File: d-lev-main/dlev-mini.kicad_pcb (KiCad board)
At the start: 4 copper layers, 175.3 x 163.3 mm, 126 parts, among them J1 S12B-PH-SM4-TB, J2 Tag-Connect TC2030-NL, J3 S8B-PH-SM4-TB, J4 S8B-PH-SM4-TB, J5 S6B-PH-SM4-TB, Q1 BSS138, Q2 BSS138, Q3 BSS138, Q4 BSS138, Q5 BSS138, SW1 RotaryEncoder_Switch, SW2 RotaryEncoder_Switch, SW3 RotaryEncoder_Switch, SW4 RotaryEncoder_Switch, SW5 RotaryEncoder_Switch, SW6 RotaryEncoder_Switch, SW7 RotaryEncoder_Switch, SW8 RotaryEncoder_Switch, U2 25LCxxx, U3 AC608, U4 AMS1117-3.3

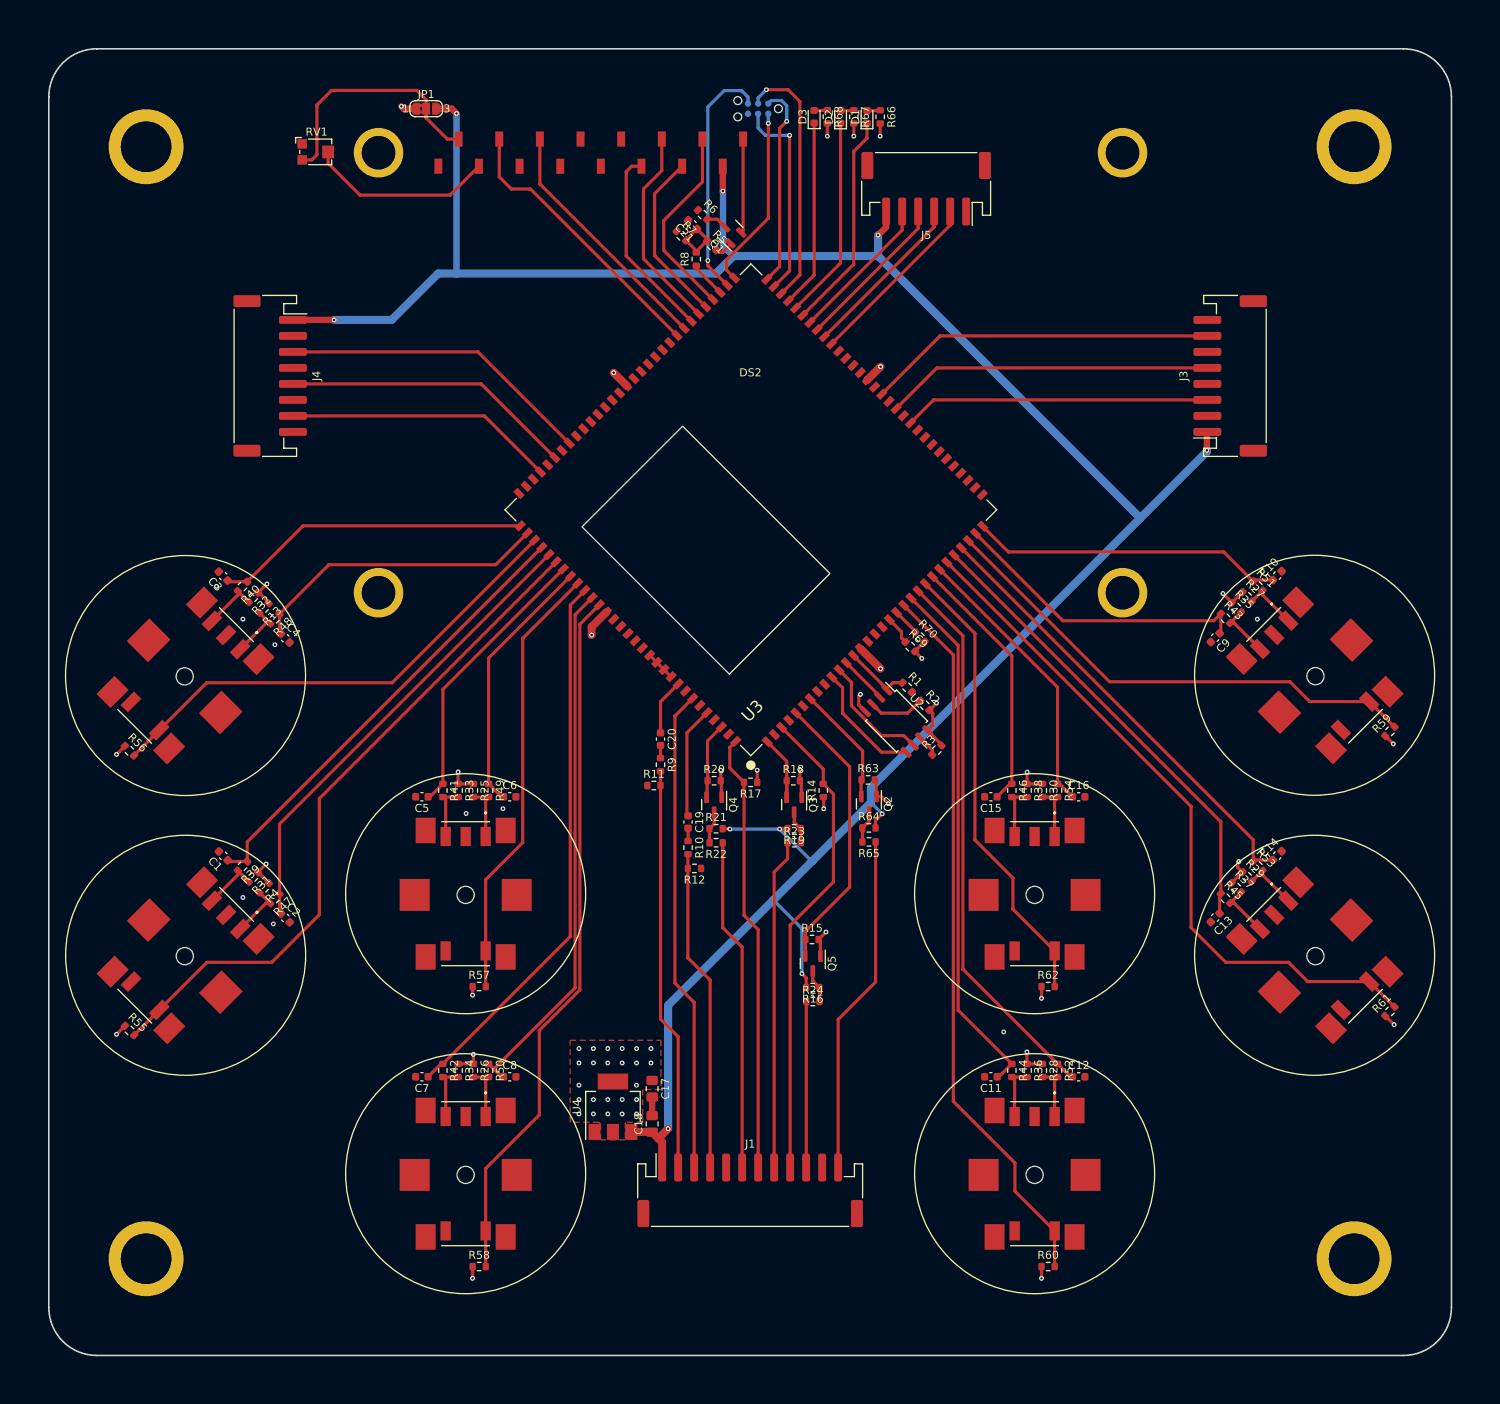
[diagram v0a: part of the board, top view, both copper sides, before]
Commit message: Via stitching around afe traces and add fix for lcd contrast pot
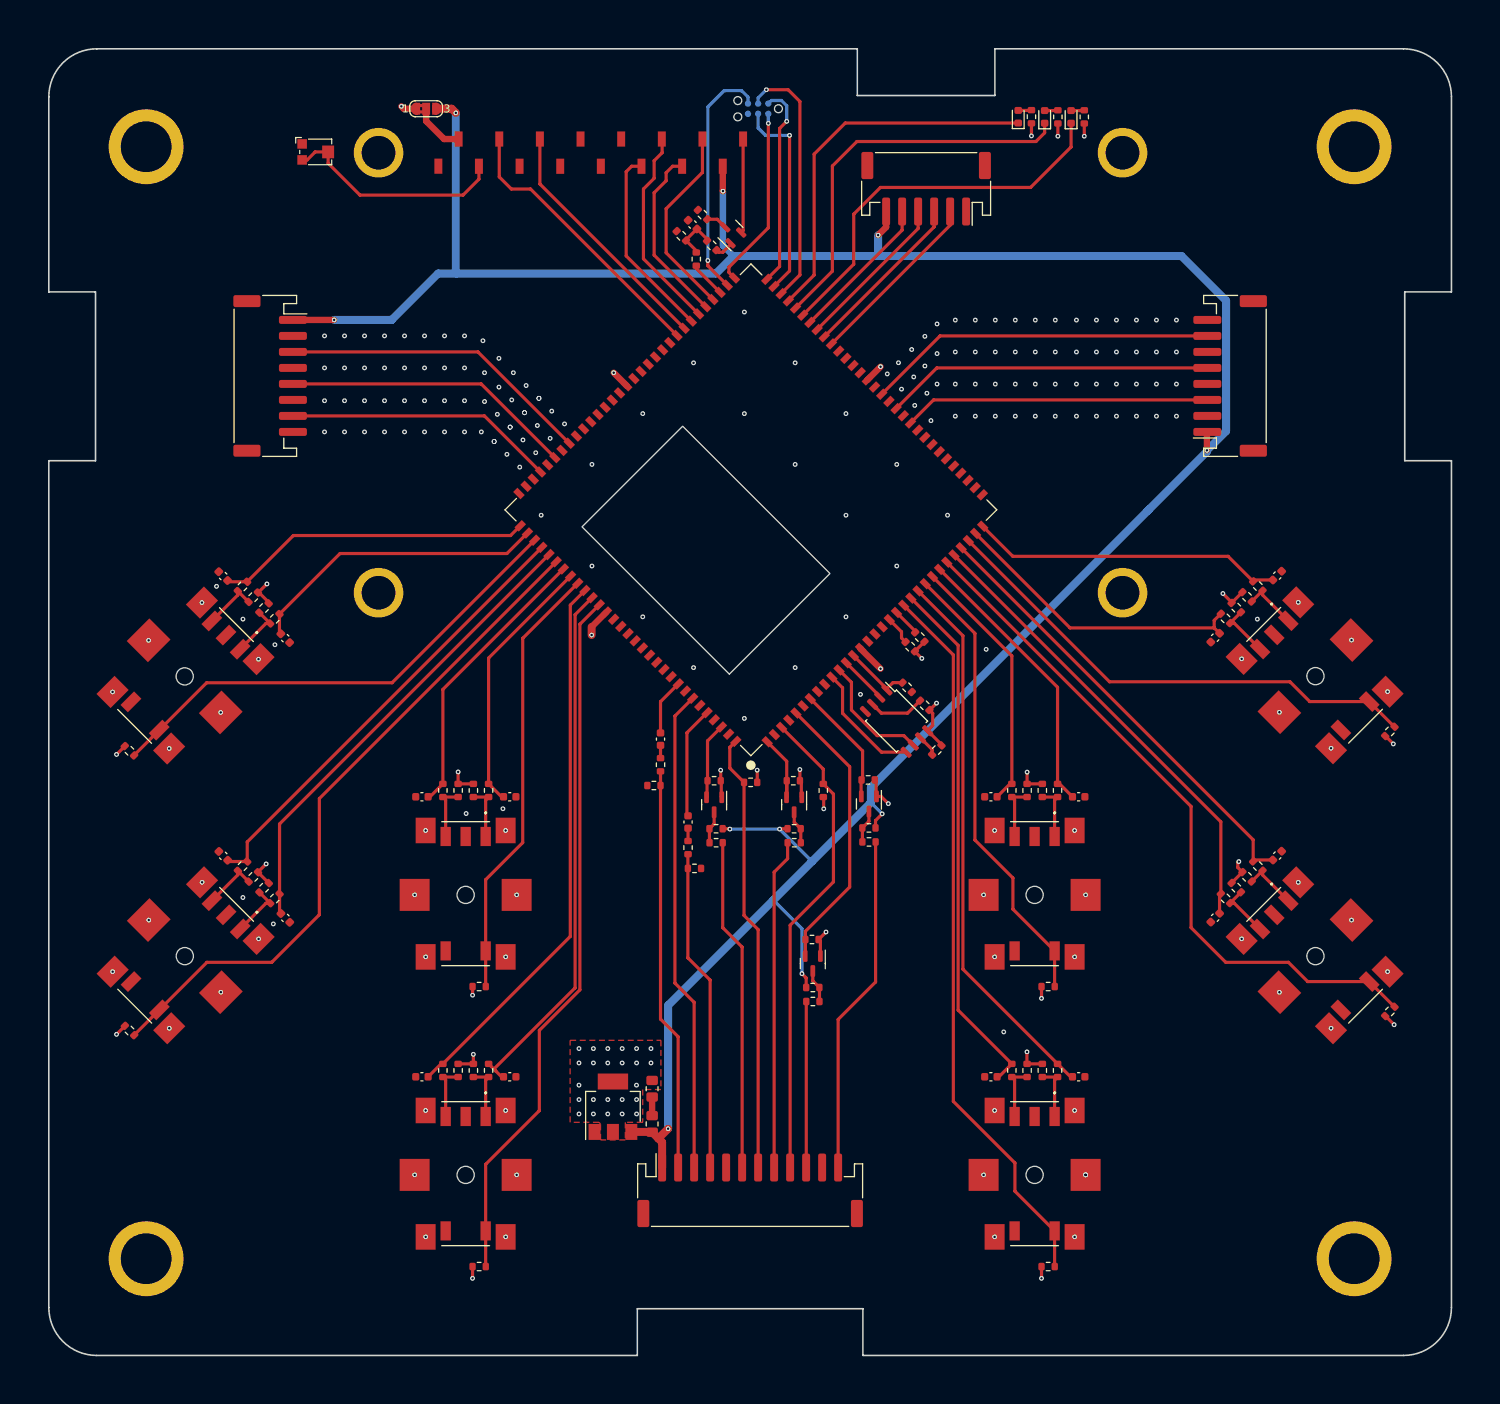
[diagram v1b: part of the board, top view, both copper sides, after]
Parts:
- moved D3 25.5 mm to (33.5, -102.0)
- moved R66 25.5 mm to (41.8, -102.0)
- moved R67 25.5 mm to (38.5, -102.0)
- moved R68 25.5 mm to (35.2, -102.0)
- moved D1 25.5 mm to (40.1, -102.0)
- moved D2 25.5 mm to (36.8, -102.0)
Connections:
- net Net-(DS2-K) renamed /LCD/backlight_cathode
- J1 pad MP2: (no net) -> unconnected-(J1-MountPin2-PadMP2)
- J5 pad MP2: (no net) -> unconnected-(J5-MountPin-PadMP2)
- RV1 pad 3: /LCD/VLCD -> Net-(DS2-V0)
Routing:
- net /LCD/VLCD: track 31.8 -> 6.54 mm
- net /FPGA/led2: track 25.4 -> 49.1 mm
- net /FPGA/led3: track 23.6 -> 46.8 mm
- net /FPGA/led1: track 27.3 -> 48.9 mm
- net +5V: track 318.2 -> 337.3 mm
- net GND: track 8.70 -> 2.32 mm, vias 10 -> 149
- net Net-(DS2-V0): track 23.4 -> 28.0 mm
- net Net-(C21-Pad1): track 7.80 -> 5.89 mm
- net /FPGA/lcd.data2: track 21.6 -> 22.4 mm
- net unconnected-(SW8-PadMP6): vias 0 -> 1
- net unconnected-(SW8-PadMP5): vias 0 -> 1
- net unconnected-(SW8-PadMP4): vias 0 -> 1
- net unconnected-(SW8-PadMP3): vias 0 -> 1
- net unconnected-(SW8-PadMP2): vias 0 -> 1
- net unconnected-(SW8-PadMP1): vias 0 -> 1
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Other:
- outline, holes or cut-outs redrawn

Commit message: many many changes'
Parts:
- removed Q1, Q3, Q4, Q5: BSS138, Package_TO_SOT_SMD:SOT-23
- removed R18, R19, R20, R21, R63, R64, R69, R70: 10k, Resistor_SMD:R_0603_1608Metric
- removed R22, R23, R24, R65: 1k, Resistor_SMD:R_0603_1608Metric
- added C22: .01u, Capacitor_SMD:C_0603_1608Metric, F.Cu at (52.4, -81.0)
- added SW10: SW_Push, Button_Switch_SMD:SW_SPST_B3U-1000P, F.Cu at (6.72, 20.5)
- added SW9: SW_Push, Button_Switch_SMD:SW_SPST_B3U-1000P, F.Cu at (52.3, -83.8)
- added TP1: 2v5, TestPoint:TestPoint_Pad_D1.0mm, B.Cu at (-19.5, -78.1)
- added TP2: 1v2, TestPoint:TestPoint_Pad_D1.0mm, B.Cu at (-17.0, -78.1)
- added TP3: 3v3, TestPoint:TestPoint_Pad_D1.0mm, B.Cu at (-19.5, -75.6)
- added TP4: GPIO_O3, TestPoint:TestPoint_Pad_D1.0mm, F.Cu at (21.0, -32.8)
- added TP5: GPIO_O2, TestPoint:TestPoint_Pad_D1.0mm, B.Cu at (21.1, -33.6)
- added TP6: GPIO_I3, TestPoint:TestPoint_Pad_D1.0mm, F.Cu at (22.8, -34.5)
- added TP7: GPIO_I2, TestPoint:TestPoint_Pad_D1.0mm, B.Cu at (22.9, -35.4)
- added TP8: VDD, TestPoint:TestPoint_Pad_D1.0mm, B.Cu at (-22.1, -78.1)
- added TP9: GND, TestPoint:TestPoint_Pad_D1.0mm, B.Cu at (-22.1, -75.6)
- J1: value S12B-PH-SM4-TB -> S6B-PH-SM4-TB; footprint d-lev:JST_PH_S12B-PH-SM4-TB_1x12-1MP_P2.00mm_Horizontal -> d-lev:JST_PH_S6B-PH-SM4-TB_1x06-1MP_P2.00mm_Horizontal
- J3: value S8B-PH-SM4-TB -> S12B-PH-SM4-TB; footprint d-lev:JST_PH_S8B-PH-SM4-TB_1x08-1MP_P2.00mm_Horizontal -> d-lev:JST_PH_S12B-PH-SM4-TB_1x12-1MP_P2.00mm_Horizontal
- J5: value S6B-PH-SM4-TB -> S8B-PH-SM4-TB; footprint d-lev:JST_PH_S6B-PH-SM4-TB_1x06-1MP_P2.00mm_Horizontal -> d-lev:JST_PH_S8B-PH-SM4-TB_1x08-1MP_P2.00mm_Horizontal
- Q2: value BSS138 -> MMBT3904
- R16: value 10k -> 1k
- moved J1 127.1 mm to (22.0, -93.0), turned to 180 degrees
- moved J4 120.0 mm to (60.0, -69.6), turned to 90 degrees
- moved J3 118.2 mm to (0.00, 32.2), turned to 0 degrees
- moved J5 85.3 mm to (-60.0, -69.6), turned to -90 degrees
- moved Q2 80.1 mm to (-0.52, -94.7), turned to 90 degrees
- moved R15 74.1 mm to (13.7, -73.0), turned to 135 degrees
- moved R16 17.2 mm to (8.93, 24.0), turned to 90 degrees
- moved R6 6.53 mm to (0.45, -91.1), turned to 90 degrees
- moved C21 6.23 mm to (-0.98, -88.4), turned to 0 degrees
- moved R5 6.12 mm to (-1.46, -91.0), turned to 90 degrees
- moved R7 5.59 mm to (-3.39, -89.1), turned to -90 degrees
- moved R8 4.84 mm to (-2.60, -86.7), turned to 0 degrees
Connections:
- C18 pad 1: +5V -> VDD
- DS2 pad 15: +5V -> VDD
- J1 pad 1: +5V -> GND
- J1 pad 2: spdif_mon -> /FPGA/tuner.oe
- J1 pad 3: mute_led -> /FPGA/tuner.le
- J1 pad 4: spdif_line -> /FPGA/tuner.sda
- J1 pad 5: GND -> /FPGA/tuner.scl
- J1 pad 6: uart_tx_5v -> VDD
- J3 pad 1: +5V -> VDD
- J3 pad 2: GND -> spdif_mon
- J3 pad 3: /FPGA/vol.quad -> mute_led
- J3 pad 4: GND -> spdif_line
- J3 pad 5: /FPGA/vol.sq -> GND
- J3 pad 6: GND -> uart_tx
- J3 pad 7: /FPGA/vol.zero -> mute_btn
- J3 pad 8: GND -> uart_rx
- J3 pad MP2: (no net) -> unconnected-(J3-MountPin2-PadMP2)
- J4 pad 1: +5V -> VDD
- J4 pad 3: /FPGA/pitch.quad -> /FPGA/vol.quad
- J4 pad 5: /FPGA/pitch.sq -> /FPGA/vol.sq
- J4 pad 7: /FPGA/pitch.zero -> /FPGA/vol.zero
- J4 pad MP2: (no net) -> unconnected-(J4-MountPin2-PadMP2)
- J5 pad 1: GND -> VDD
- J5 pad 2: /FPGA/tuner.oe -> GND
- J5 pad 3: /FPGA/tuner.le -> /FPGA/pitch.quad
- J5 pad 4: /FPGA/tuner.sda -> GND
- J5 pad 5: /FPGA/tuner.scl -> /FPGA/pitch.sq
- J5 pad 6: +5V -> GND
- JP1 pad 3: +5V -> VDD
- Q2 pad 1: +3V3 -> Net-(Q2-B)
- Q2 pad 2: /midi_rx -> Net-(Q2-E)
- Q2 pad 3: Net-(Q2-D) -> /LCD/backlight_cathode
- R15 pad 1: /midi_tx -> /FPGA/~{reset}
- R16 pad 1: Net-(Q5-D) -> GND
- R16 pad 2: +5V -> Net-(R16-Pad2)
- R5 pad 2: Net-(Q1-G) -> Net-(Q2-B)
- R6 pad 2: Net-(Q1-D) -> Net-(Q2-E)
- U3 pad 1: /uart_rx_3v -> uart_rx
- U3 pad 122: /uart_tx_3v -> uart_tx
- U3 pad 5: /midi_tx -> midi_out
- U3 pad 7: /midi_rx -> midi_in
- U3 pad 74: +1V2 -> Net-(U3-VDD1.2)
- U4 pad 3: +5V -> VDD
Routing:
- net VDD: track 0.00 -> 340.8 mm, vias 0 -> 7
- net +5V: track 337.3 -> 0.00 mm, vias 10 -> 0
- net uart_tx: track 0.00 -> 56.9 mm
- net uart_rx: track 0.00 -> 55.0 mm
- net /FPGA/~{reset}: track 0.00 -> 46.4 mm
- net uart_tx_5v: track 41.6 -> 0.00 mm
- net uart_rx_5v: track 41.3 -> 0.00 mm
- net midi_out: track 20.8 -> 61.8 mm
- net /midi_tx: track 35.5 -> 0.00 mm
- net +2V5: track 22.9 -> 44.7 mm, vias 1 -> 2
- net GND: track 2.32 -> 23.9 mm, vias 149 -> 195
- net midi_in: track 42.6 -> 62.9 mm
- net /midi_rx: track 14.9 -> 0.00 mm
- net /uart_rx_3v: track 10.0 -> 0.00 mm
- net /uart_tx_3v: track 9.55 -> 0.00 mm
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
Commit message: many more changes
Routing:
- net VDD: track 340.8 -> 20.9 mm, vias 7 -> 9
- net GND: track 23.9 -> 25.7 mm, vias 195 -> 210
- net +3V3: track 74.0 -> 73.6 mm, vias 54 -> 50
- added copper zone on B.Cu, net VDD
- added copper zone on F.Cu, net VDD
- removed copper zone on B.Cu, net GND

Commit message: round tracks and teardrops
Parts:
- added R34: 100, Resistor_SMD:R_0603_1608Metric, F.Cu at (86.8, 125.5)
- added R35: 100, Resistor_SMD:R_0603_1608Metric, F.Cu at (90.8, 125.5)
- added R59: 100, Resistor_SMD:R_0603_1608Metric, F.Cu at (94.9, 125.5)
- added R60: 0, Resistor_SMD:R_0603_1608Metric, F.Cu at (98.8, 125.5)
- added TP10: TestPoint, TestPoint:TestPoint_Pad_D1.0mm, B.Cu at (76.8, 144.9)
- added TP11: TestPoint, TestPoint:TestPoint_Pad_D1.0mm, B.Cu at (78.8, 144.9)
- added TP12: TestPoint, TestPoint:TestPoint_Pad_D1.0mm, B.Cu at (80.8, 144.9)
- added TP13: TestPoint, TestPoint:TestPoint_Pad_D1.0mm, B.Cu at (82.8, 144.9)
- added TP14: TestPoint, TestPoint:TestPoint_Pad_D1.0mm, B.Cu at (84.8, 144.9)
- added TP15: TestPoint, TestPoint:TestPoint_Pad_D1.0mm, B.Cu at (86.8, 144.9)
- added TP16: TestPoint, TestPoint:TestPoint_Pad_D1.0mm, B.Cu at (88.8, 144.9)
- added TP17: TestPoint, TestPoint:TestPoint_Pad_D1.0mm, B.Cu at (90.8, 144.9)
- added TP18: TestPoint, TestPoint:TestPoint_Pad_D1.0mm, B.Cu at (92.8, 144.9)
- added TP19: TestPoint, TestPoint:TestPoint_Pad_D1.0mm, B.Cu at (94.8, 144.9)
- added TP20: TestPoint, TestPoint:TestPoint_Pad_D1.0mm, B.Cu at (96.8, 144.9)
- added TP21: TestPoint, TestPoint:TestPoint_Pad_D1.0mm, B.Cu at (98.8, 144.9)
- moved C1 141.3 mm to (86.9, 22.3)
- moved C10 141.3 mm to (46.8, 93.7)
- moved C11 141.3 mm to (57.8, 93.7)
- moved C12 141.3 mm to (80.1, 96.8)
- moved C13 141.3 mm to (117.9, 93.7)
- moved C14 141.3 mm to (128.9, 93.7)
- moved C15 141.3 mm to (153.7, 101.0)
- moved C16 141.3 mm to (146.0, 108.8)
- moved C17 141.3 mm to (57.8, 128.7)
- moved C18 141.3 mm to (46.8, 128.7)
- moved C19 141.3 mm to (75.6, 130.2)
- moved C2 141.3 mm to (140.2, 29.7)
- moved C20 141.3 mm to (75.6, 134.6)
- moved C21 141.3 mm to (117.9, 128.7)
- moved C22 141.3 mm to (128.9, 128.7)
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- renumbered C21 to C1, C5 to C10, C6 to C11, C19 to C12, C15 to C13, C16 to C14, C14 to C15, C13 to C16, C8 to C17, C7 to C18, C17 to C19, C22 to C2, C18 to C20, C11 to C21, C12 to C22, C4 to C3, C3 to C4, C20 to C5, C10 to C6, C9 to C7, C1 to C8, C2 to C9, D3 to D1, D1 to D2, D2 to D3, DS2 to DS1, H4 to H1, H3 to H2, H6 to H3, H5 to H4, H7 to H5, H8 to H6, H2 to H7, H1 to H8, J5 to J2, J4 to J3, J3 to J4, J2 to J5, Q2 to Q1, R66 to R1, R40 to R10, R13 to R11, R48 to R12, R32 to R13, R2 to R14, R1 to R15, R3 to R16, R27 to R17, R35 to R18, R43 to R19, R67 to R2, R51 to R20, R59 to R21, R39 to R22, R47 to R23, R31 to R24, R4 to R25, R25 to R26, R49 to R27, R33 to R28, R41 to R29, R68 to R3, R10 to R30, R12 to R31, R9 to R32, R11 to R33, R17 to R34, R14 to R35, R54 to R36, R38 to R37, R46 to R38, R30 to R39, R7 to R4, R29 to R40, R45 to R41, R53 to R42, R37 to R43, R55 to R44, R50 to R45, R34 to R46, R26 to R47, R42 to R48, R57 to R49, R6 to R5, R16 to R50, R52 to R51, R62 to R52, R28 to R53, R36 to R54, R44 to R55, R61 to R56, R58 to R57, R60 to R58, R8 to R6, R5 to R7, R15 to R8, R56 to R9, SW9 to SW1, SW6 to SW10, SW5 to SW3, SW1 to SW4, SW3 to SW5, SW8 to SW6, SW10 to SW8, SW4 to SW9, TP4 to TP1, TP6 to TP2, TP1 to TP3, TP8 to TP4, TP9 to TP5, TP2 to TP6, TP3 to TP7, TP5 to TP8, TP7 to TP9, U3 to U1, U4 to U3
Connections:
- J4 pad 10: midi_out -> Net-(J4-Pin_10)
- J4 pad 12: midi_in -> Net-(J4-Pin_12)
- J4 pad 6: uart_tx -> Net-(J4-Pin_6)
- J4 pad 8: uart_rx -> Net-(J4-Pin_8)
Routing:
- net Net-(J4-Pin_10): track 0.00 -> 18.6 mm, vias 0 -> 1
- net Net-(J4-Pin_6): track 0.00 -> 18.6 mm, vias 0 -> 1
- net Net-(J4-Pin_12): track 0.00 -> 18.6 mm, vias 0 -> 1
- net Net-(J4-Pin_8): track 0.00 -> 18.6 mm, vias 0 -> 1
- net midi_out: track 61.8 -> 45.7 mm
- net midi_in: track 62.9 -> 46.9 mm
- net uart_tx: track 56.9 -> 40.9 mm
- net uart_rx: track 55.0 -> 39.1 mm
- net GND: track 25.7 -> 33.0 mm
- net VDD: track 20.9 -> 25.6 mm, vias 9 -> 10
- net spdif_mon: track 50.4 -> 54.9 mm, vias 0 -> 1
- net spdif_line: track 40.3 -> 44.7 mm, vias 0 -> 1
- net mute_btn: track 55.0 -> 59.4 mm, vias 0 -> 1
- net mute_led: track 60.6 -> 64.9 mm, vias 0 -> 1
- net acal_btn: track 59.9 -> 64.1 mm, vias 0 -> 1
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
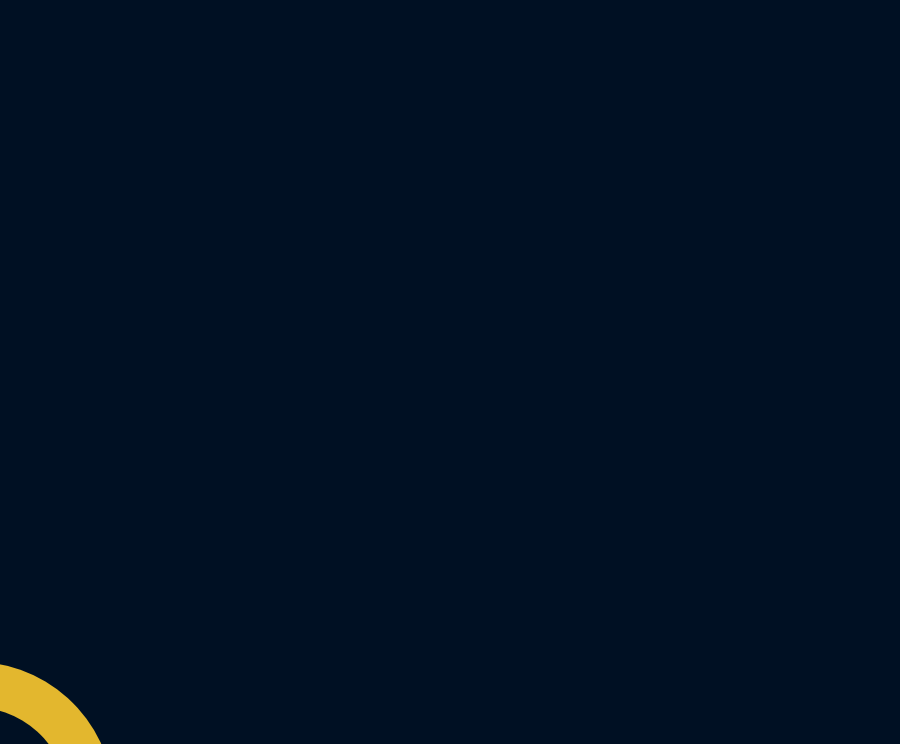
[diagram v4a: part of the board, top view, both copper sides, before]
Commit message: Aesthetic improvements to main/AFE
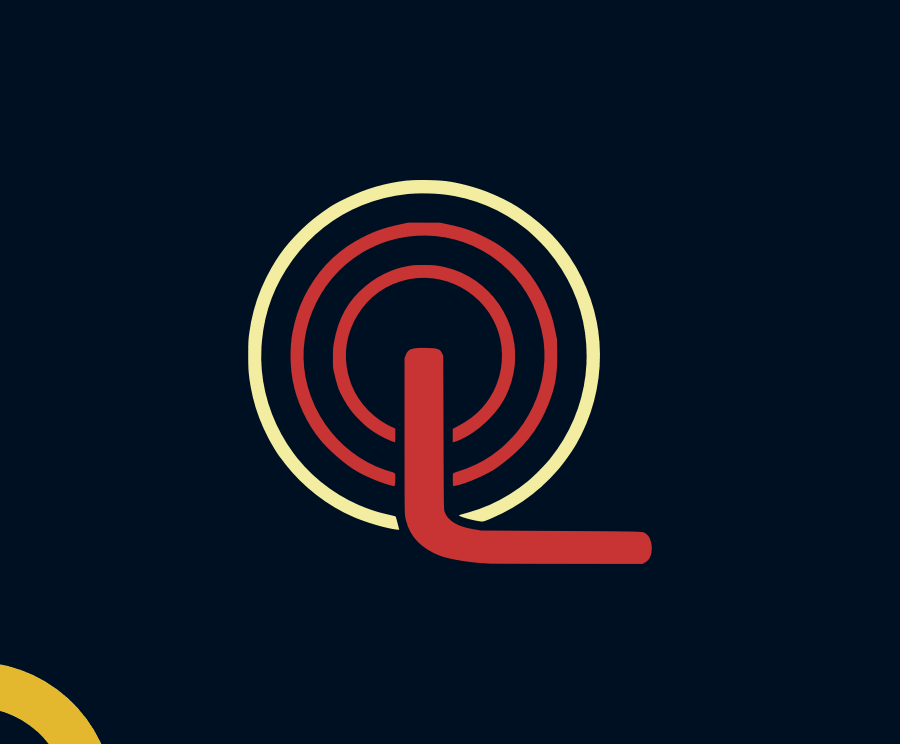
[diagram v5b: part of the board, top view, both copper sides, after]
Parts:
- added G***: LOGO, d-lev:logo, F.Cu at (27.4, 136.3)
